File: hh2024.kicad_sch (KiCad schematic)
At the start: 55 parts, among them J1 SAO, J2 Breakout pads, J3 Micro_SD_Card, J4 USB-C, K1 SANYOU_SRD_Form_C, Q3 AP2302B, SW1 Multi-Directional-Switches, SW2 Multi-Directional-Switches, SW3 Multi-Directional-Switches, SW4 Multi-Directional-Switches, SW5 Multi-Directional-Switches, U5 CH32V003F4U6

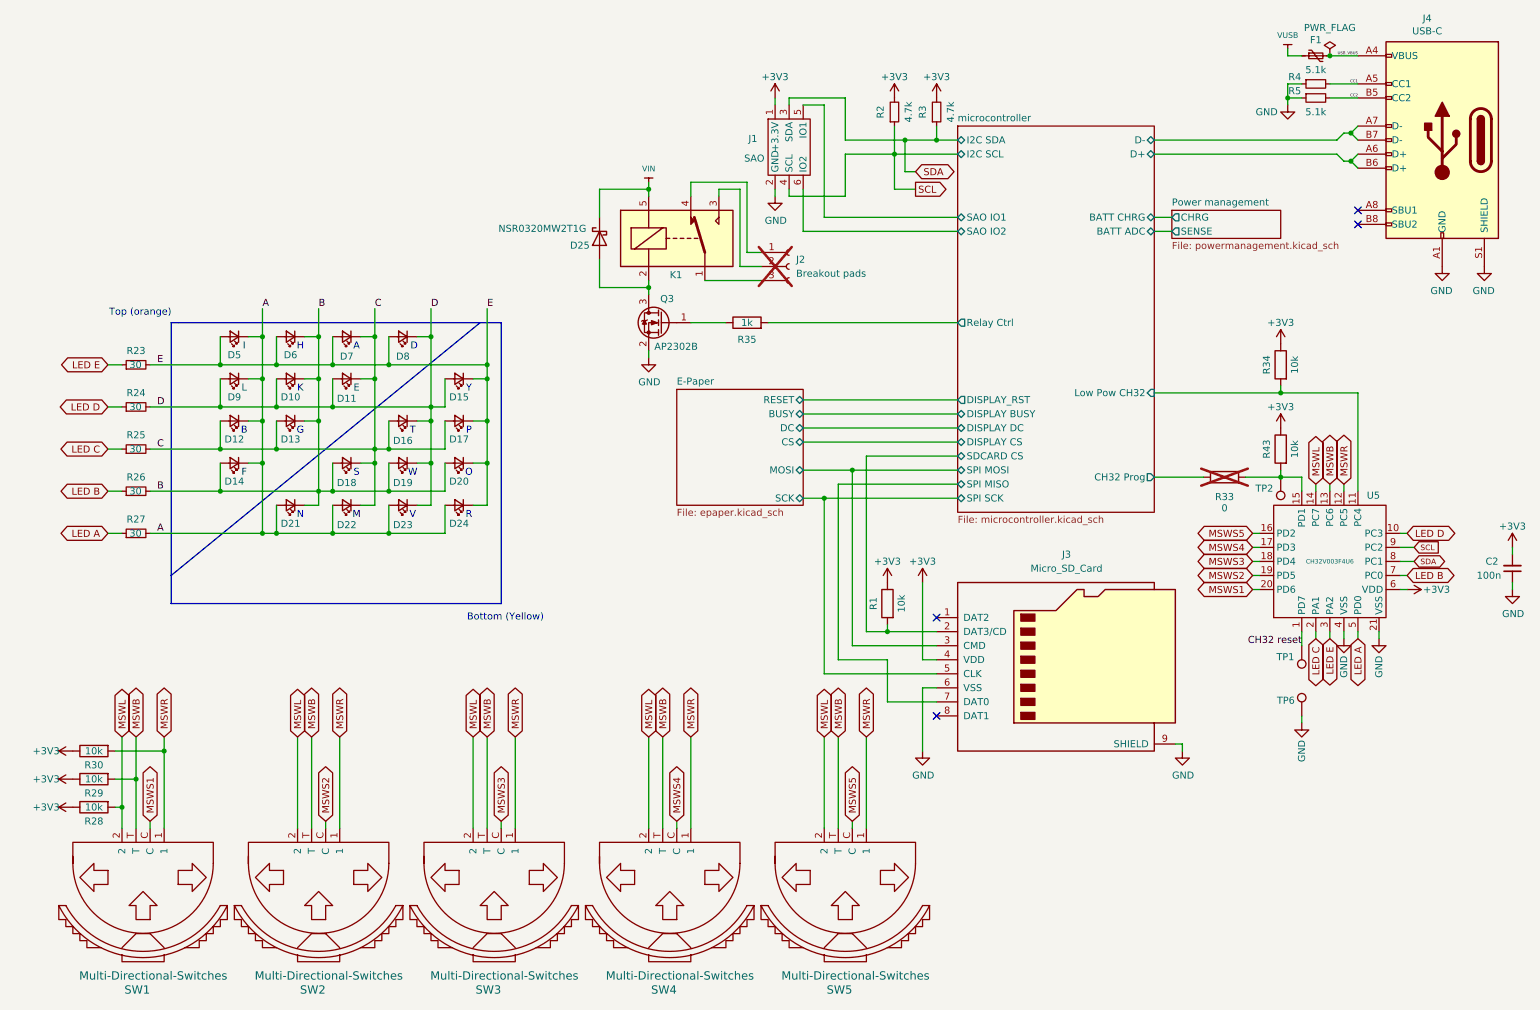
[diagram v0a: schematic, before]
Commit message: V1.1 almost complete update
✔️add a 100k resistor between the gate of the FET in the epaper circuit and ground
✔️Moved LEDs to match the alignment on line “HIKL” and “Y”
✔️Change polarity on the LEDs, they are the “wrong way around” (software thing only, doesn’t matter for charlieplexing
-Add relay control on PD7 (if it can be changed)
✔️Swap PA1 and PA2 with PD3 and PD2
✔️ Prog pads for CH32
✔️Connect SAO IOs to relay output (to make an add-on glow when the relay ticks), pulled low by default.
✔️ Move relay
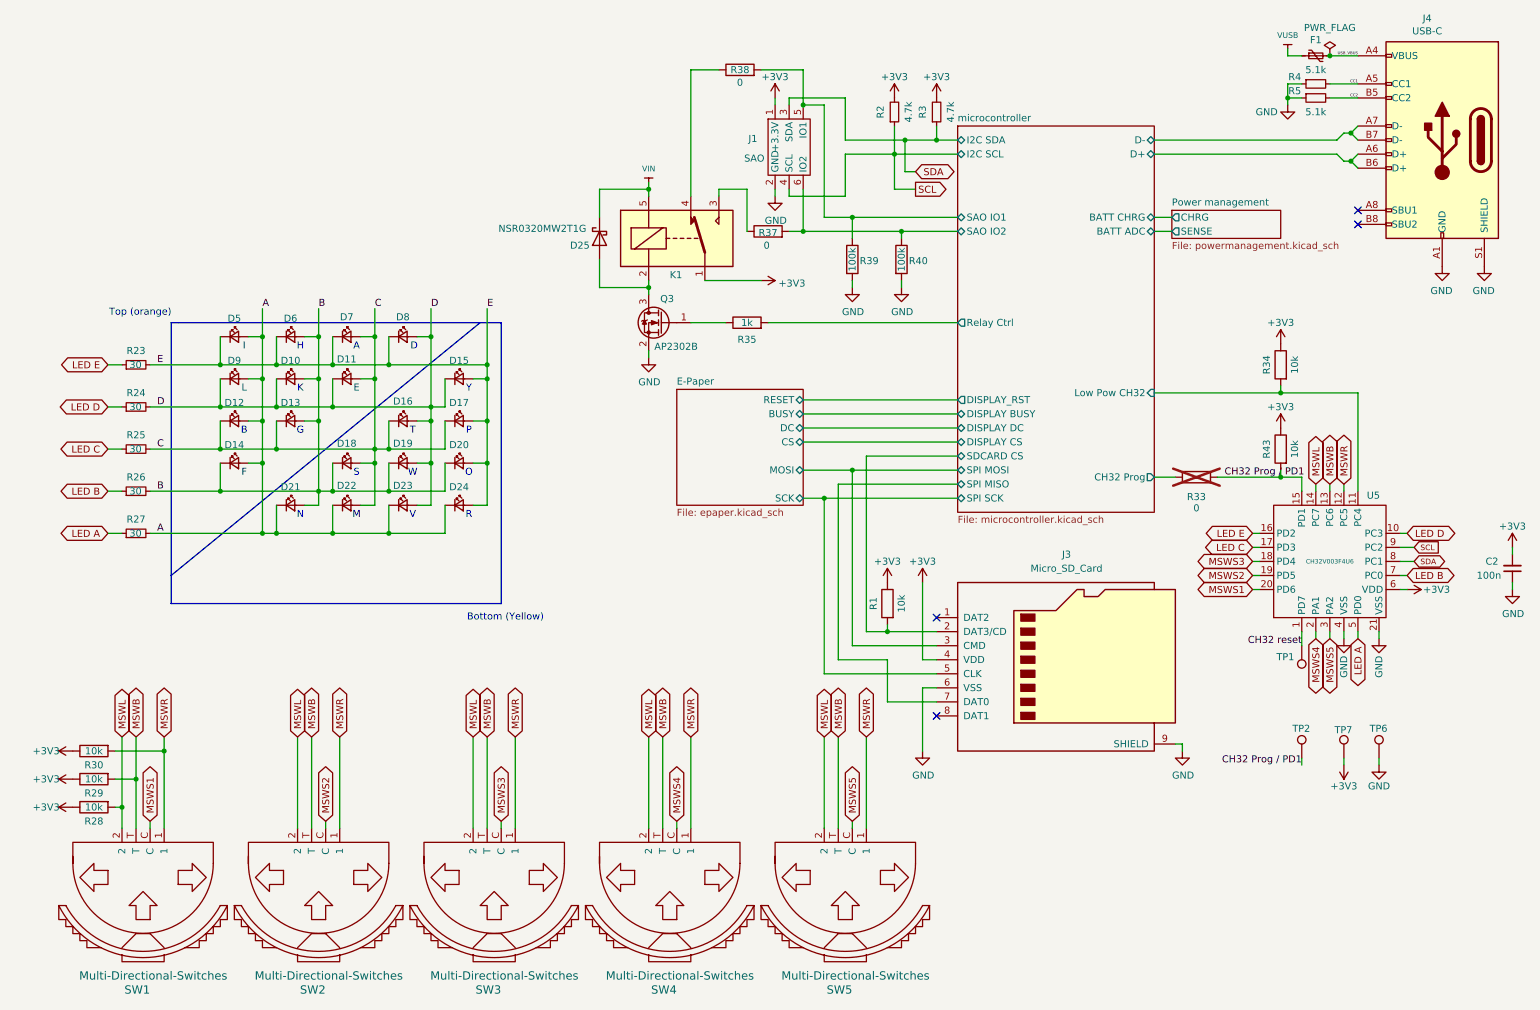
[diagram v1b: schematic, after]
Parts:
- removed J2: Breakout pads, Connector_PinHeader_2.54mm:PinHeader_1x03_P2.54mm_Vertical, symbol Connector:Conn_01x03_Socket
- added R37, R38: 0, Resistor_SMD:R_0805_2012Metric, symbol symbols:R
- added R39, R40: 100k, Resistor_SMD:R_0805_2012Metric, symbol symbols:R
- added TP7: TestPoint, TestPoint:TestPoint_Pad_2.0x2.0mm, symbol Connector:TestPoint
- TP2, TP6: footprint TestPoint:TestPoint_Pad_1.0x1.0mm -> TestPoint:TestPoint_Pad_2.0x2.0mm
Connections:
- net +3V3: now also K1.1, TP7.1
- net A: now also D12.2 (A), D14.2 (A), D21.1 (K), D22.1 (K), D23.1 (K), D24.1 (K), D5.2 (A), D9.2 (A); no longer D12.1 (K), D14.1 (K), D21.2 (A), D22.2 (A), D23.2 (A), D24.2 (A), D5.1 (K), D9.1 (K)
- net B: now also D10.2 (A), D13.2 (A), D14.1 (K), D18.1 (K), D19.1 (K), D20.1 (K), D21.2 (A), D6.2 (A); no longer D10.1 (K), D13.1 (K), D14.2 (A), D18.2 (A), D19.2 (A), D20.2 (A), D21.1 (K), D6.1 (K)
- net C: now also D11.2 (A), D12.1 (K), D13.1 (K), D16.1 (K), D17.1 (K), D18.2 (A), D22.2 (A), D7.2 (A); no longer D11.1 (K), D12.2 (A), D13.2 (A), D16.2 (A), D17.2 (A), D18.1 (K), D22.1 (K), D7.1 (K)
- net D: now also D10.1 (K), D11.1 (K), D15.1 (K), D16.2 (A), D19.2 (A), D23.2 (A), D8.2 (A), D9.1 (K); no longer D10.2 (A), D11.2 (A), D15.2 (A), D16.1 (K), D19.1 (K), D23.1 (K), D8.1 (K), D9.2 (A)
- net E: now also D15.2 (A), D17.2 (A), D20.2 (A), D24.2 (A), D5.1 (K), D6.1 (K), D7.1 (K), D8.1 (K); no longer D15.1 (K), D17.1 (K), D20.1 (K), D24.1 (K), D5.2 (A), D6.2 (A), D7.2 (A), D8.2 (A)
- net GND: now also R39.2, R40.2
- net LED C: now also U5.17 (PD3); no longer U5.2 (PA1)
- net LED E: now also U5.16 (PD2); no longer U5.3 (PA2)
- net MSWS4: now also U5.2 (PA1); no longer U5.17 (PD3)
- net MSWS5: now also U5.3 (PA2); no longer U5.16 (PD2)
- net microcontroller/SAO IO1: now also R38.2, R39.1
- net microcontroller/SAO IO2: now also R37.2, R40.1
- net CH32 Prog / PD1: now reaches R33.2, R43.2, TP2.1, U5.15 (PD1)
- net at K1.4: now also R38.1
- net at K1.3: now also R37.1
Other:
- moved on the sheet: D10, D11, D12, D13, D14, D15, D16, D17, D18, D19, D20, D21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

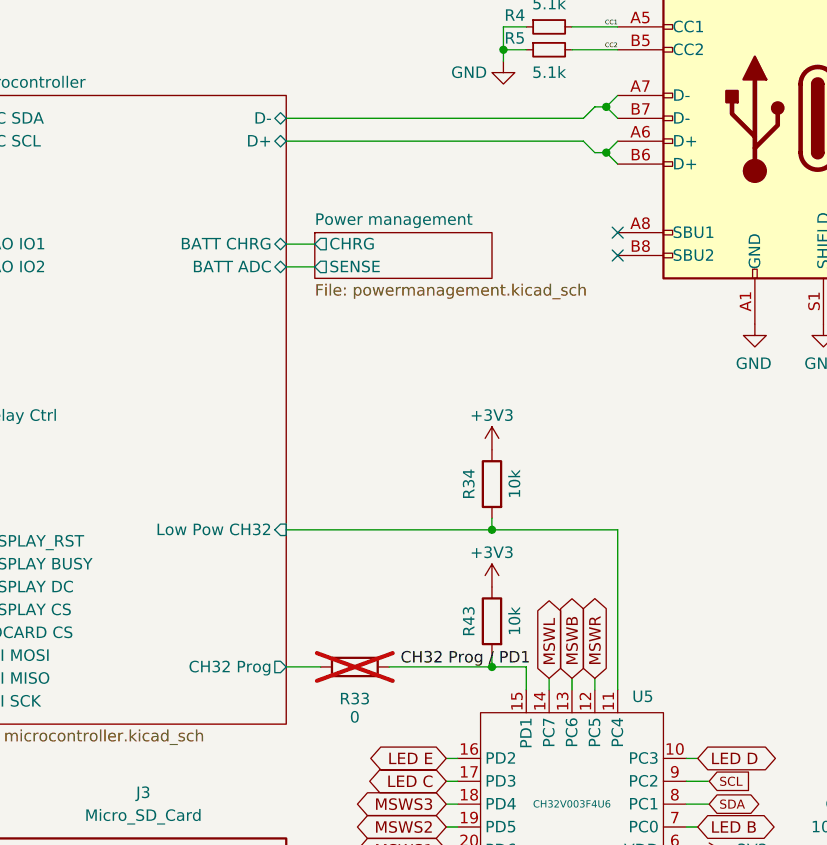
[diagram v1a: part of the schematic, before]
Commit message: V1.2
added reverse mount RGB LED
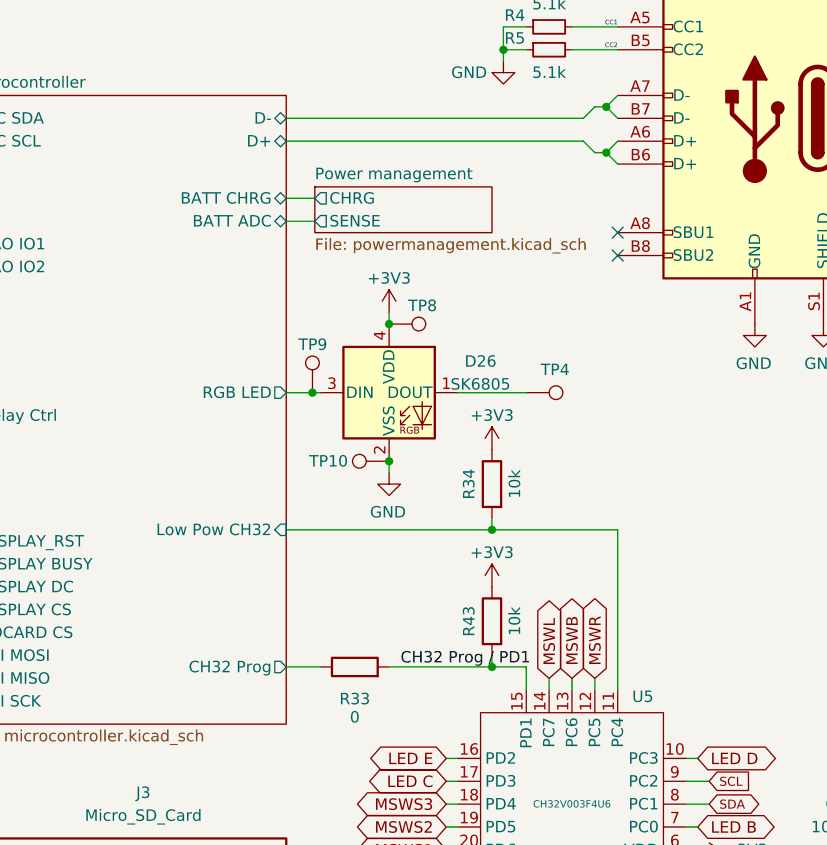
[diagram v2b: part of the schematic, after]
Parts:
- added D26: SK6805, BamboulabFootprints:SK6805-EC3210R, symbol LED:SK6805
- added TP10, TP4, TP8, TP9: TestPoint, TestPoint:TestPoint_Pad_1.0x1.0mm, symbol Connector:TestPoint
- R33: now fitted
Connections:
- net +3V3: now also D26.4 (VDD), TP8.1
- net GND: now also D26.2 (VSS), TP10.1
- new net: D26.1 (DOUT), TP4.1
- new net microcontroller/RGB LED: D26.3 (DIN), TP9.1
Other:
- sheet microcontroller ports: added RGB LED; removed none

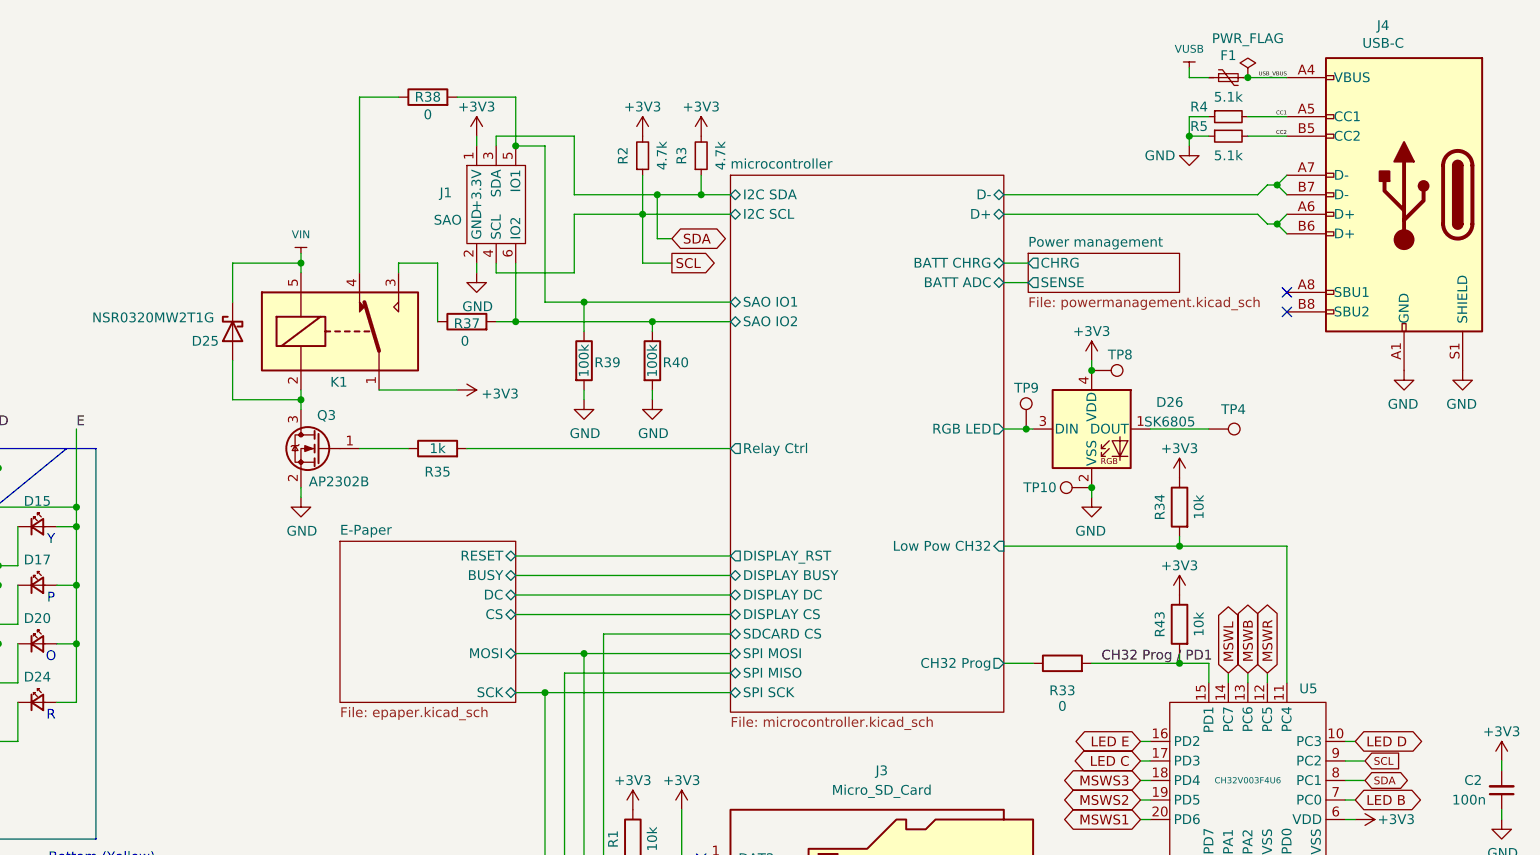
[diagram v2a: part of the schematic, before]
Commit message: V1.3
Changed C23 from 1uF to 0.47uF
Changed R21 from 27ohms to 2.2ohms
Changed C17 from 4.7uF to 1uF
Removed R37 and R38, R39 and R40
Added J2 QWIIC connector
Added U6 buffer to drive SK6085 LED
Removed R33 to a direct wire connection
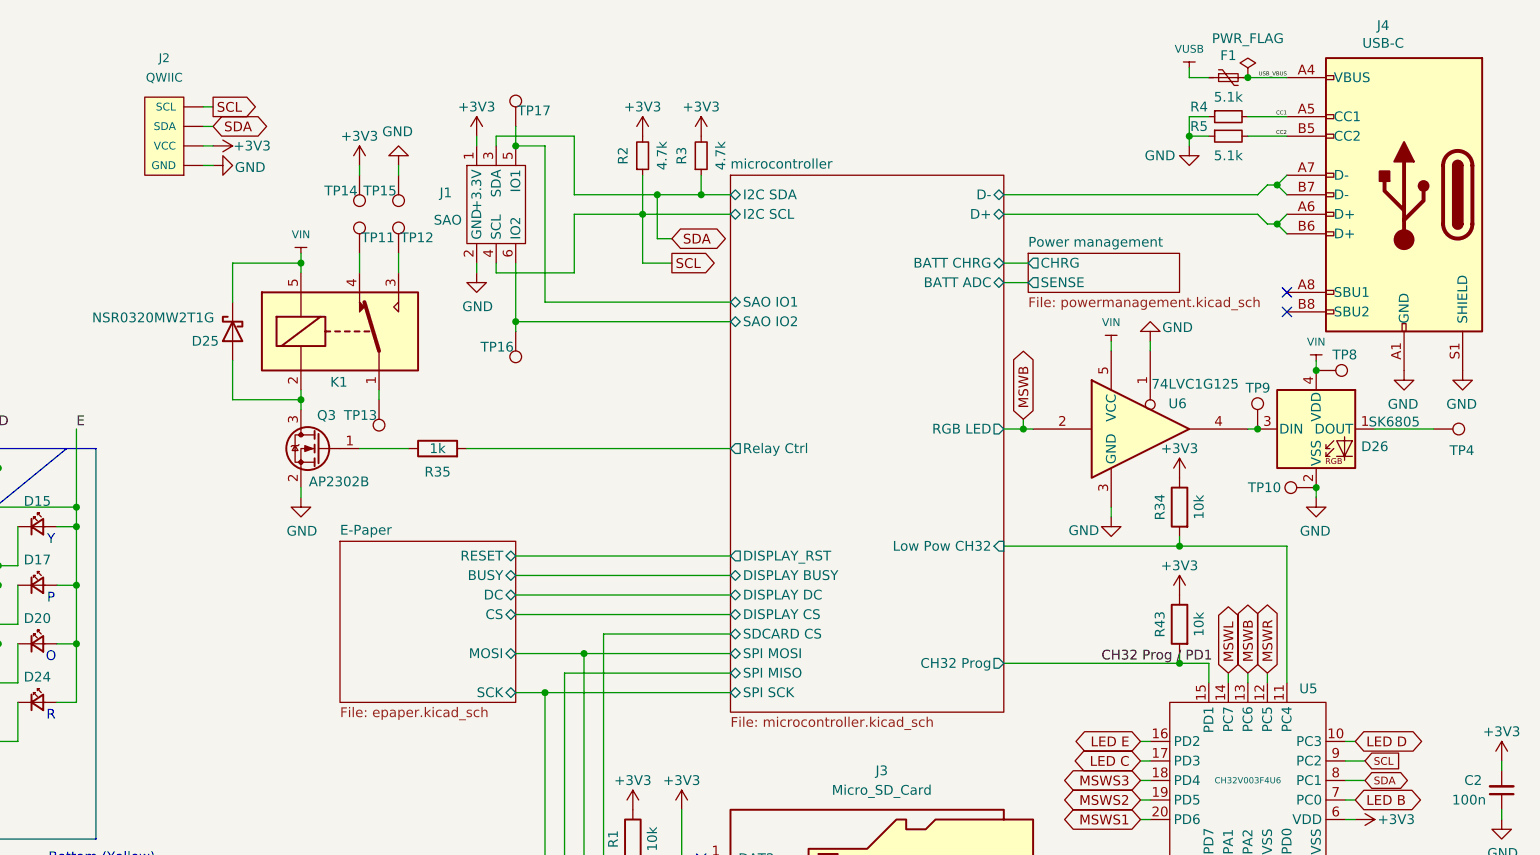
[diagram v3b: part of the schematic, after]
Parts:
- removed R33, R37, R38: 0, Resistor_SMD:R_0805_2012Metric, symbol symbols:R
- removed R39, R40: 100k, Resistor_SMD:R_0805_2012Metric, symbol symbols:R
- added J2: QWIIC, BamboulabFootprints:Qwiic 1X04_1MM_RA_GND, symbol bambouLab:qwiic
- added TP11, TP12, TP13, TP14, TP15, TP16, TP17: TestPoint, TestPoint:TestPoint_Pad_1.0x1.0mm, symbol Connector:TestPoint
- added U6: 74LVC1G125, Package_TO_SOT_SMD:SOT-353_SC-70-5, symbol 74xGxx:74LVC1G125
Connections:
- net +3V3: now also J2.2 (VCC), TP14.1; no longer D26.4 (VDD), K1.1, TP8.1
- net GND: now also J2.1 (GND), J2.5, J2.6, TP15.1, U6.1, U6.3 (GND)
- net MSWB: now also U6.2
- net SCL: now also J2.4 (SCL)
- net SDA: now also J2.3 (SDA)
- net VIN: now also D26.4 (VDD), TP8.1, U6.5 (VCC)
- net microcontroller/SAO IO1: now also TP17.1
- net microcontroller/SAO IO2: now also TP16.1
- net at K1.4: now also TP11.1
- net at K1.3: now also TP12.1
- net microcontroller/RGB LED: no longer names the net of D26.3 (DIN), TP9.1
- net microcontroller/RGB LED: now also U6.4
- new net: K1.1, TP13.1
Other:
- moved on the sheet: D26, TP10, TP4, TP8, TP9

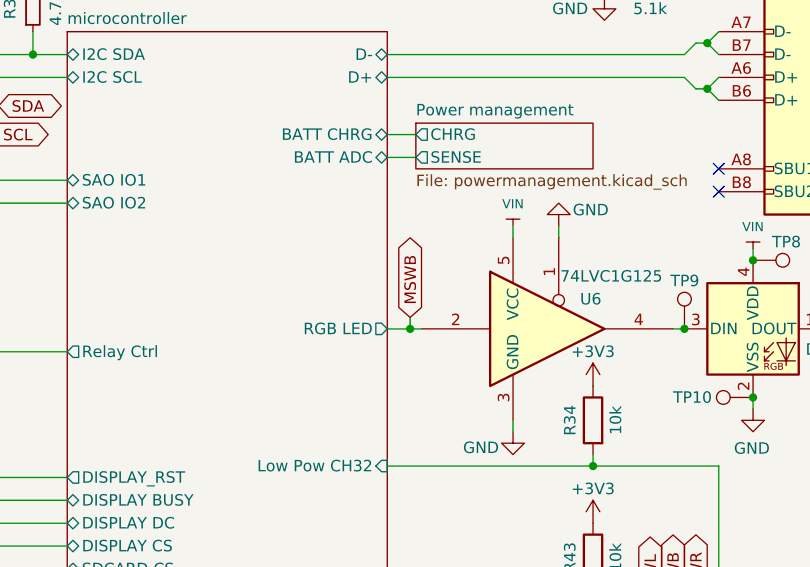
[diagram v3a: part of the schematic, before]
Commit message: removed connection from LEDs to CH32
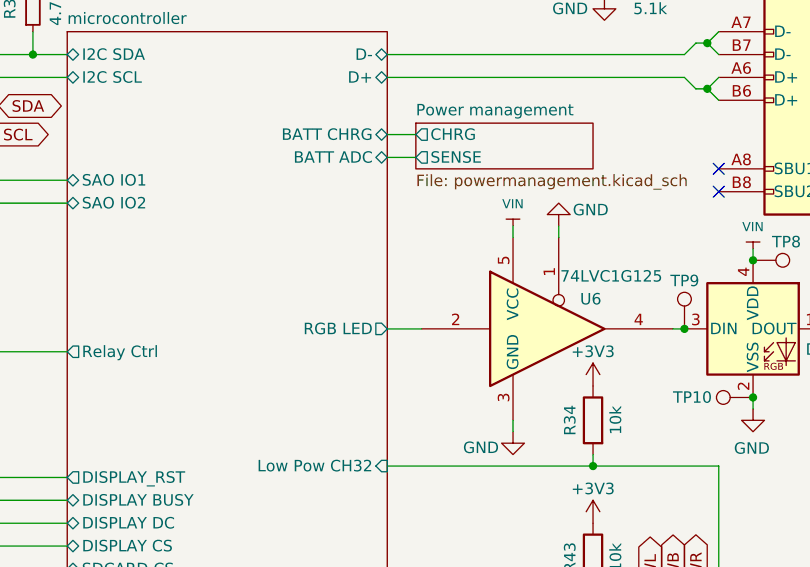
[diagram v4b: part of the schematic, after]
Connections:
- net MSWB: no longer U6.2
- new net microcontroller/RGB LED: U6.2
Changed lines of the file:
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@@
   (junction (at 238.76 83.82) (diameter 0) (color 0 0 0 0)
-  )
-  (junction (at 218.44 68.58) (diameter 0) (color 0 0 0 0)
   )
   (junction (at 54.61 81.28) (diameter 0) (color 0 0 0 0)
@@
     (stroke (width 0) (type default))
   )
-  (wire (pts (xy 215.9 68.58) (xy 218.44 68.58))
+  (wire (pts (xy 215.9 68.58) (xy 219.71 68.58))
     (stroke (width 0) (type default))
   )
@@
     (stroke (width 0) (type default))
   )
-  (wire (pts (xy 218.44 67.31) (xy 218.44 68.58))
-    (stroke (width 0) (type default))
-  )
   (wire (pts (xy 170.815 38.1) (xy 170.815 43.815))
     (stroke (width 0) (type default))
@@
   )
   (wire (pts (xy 260.35 119.38) (xy 261.62 119.38))
-    (stroke (width 0) (type default))
-  )
-  (wire (pts (xy 218.44 68.58) (xy 219.71 68.58))
     (stroke (width 0) (type default))
   )
@@
       (effects (font (size 1.27 1.27)) (justify left) hide)
     )
-  )
-  (global_label "MSWB" (shape bidirectional) (at 218.44 67.31 90) (fields_autoplaced)
-    (effects (font (size 1.27 1.27)) (justify left))
-    (property "Intersheetrefs" "${INTERSHEET_REFS}" (at 218.44 58.9584 90)
-      (effects (font (size 1.27 1.27)) (justify left) hide)
-    )
